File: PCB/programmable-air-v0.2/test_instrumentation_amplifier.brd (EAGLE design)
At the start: 100 x 80 mm, 15 parts, among them IC1 INA126U, IC2 7805T

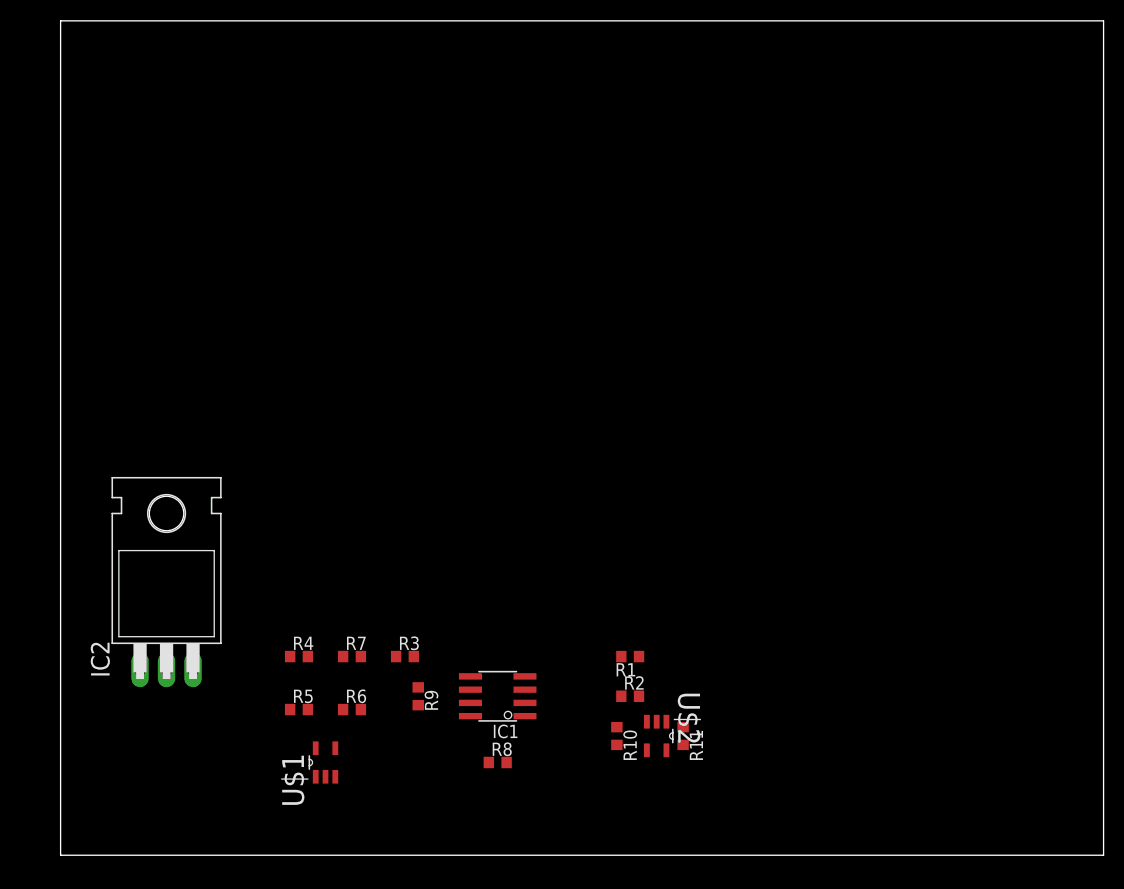
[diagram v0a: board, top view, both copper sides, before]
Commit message: Working towards instrumentation amplifier instead of HX711
MCP6001 was a huge mistake. 6V Vin max. Modifying circuit to LM358.
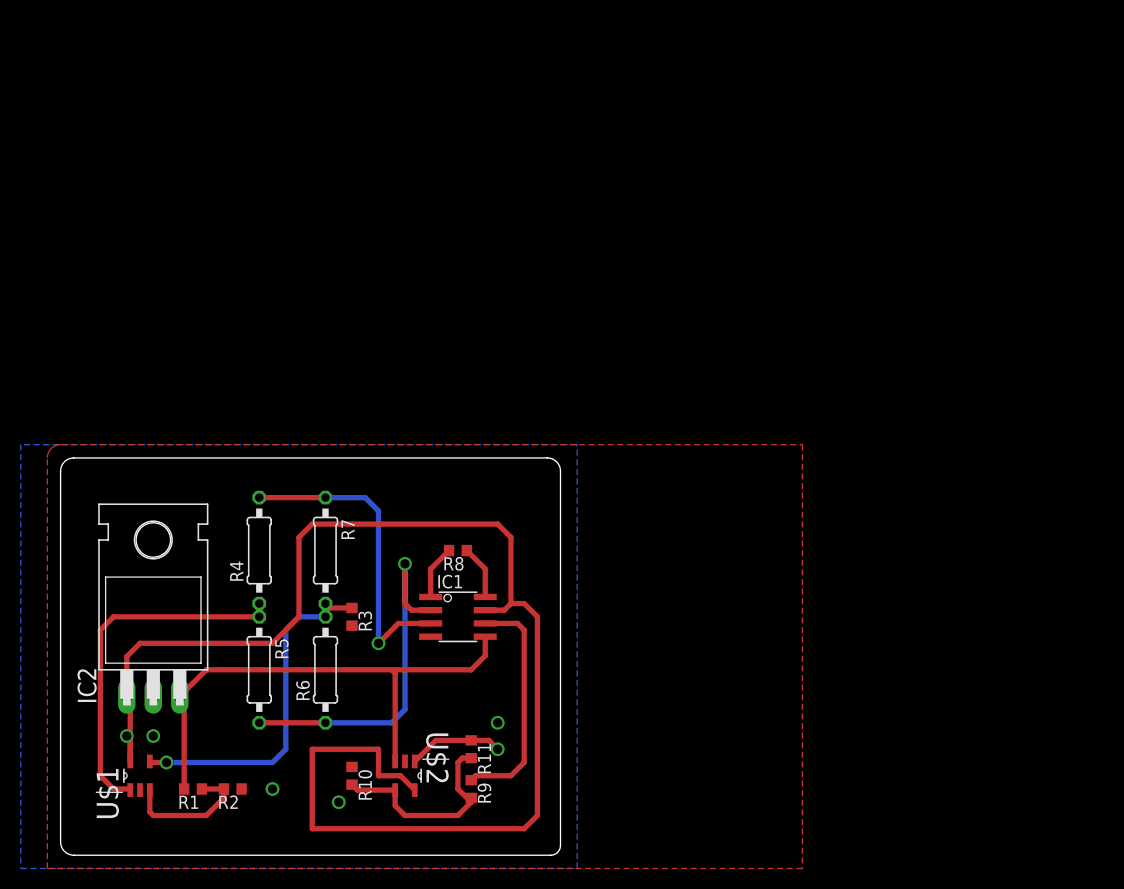
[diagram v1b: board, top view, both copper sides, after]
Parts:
- R4, R5, R6, R7: device eagle-ltspice:R0603 -> eagle-ltspice:0207/10
- moved R1 43.8 mm to (12.7, 6.35)
- moved R2 39.1 mm to (16.5, 6.35), turned to 180 degrees
- moved R10 25.7 mm to (27.9, 7.62)
- moved U$2 24.4 mm to (33.0, 7.62)
- moved R8 20.7 mm to (38.1, 29.2), turned to 180 degrees
- moved R11 20.4 mm to (39.4, 10.2)
- moved U$1 17.8 mm to (7.62, 7.62)
- moved R4 10.9 mm to (19.1, 29.2), turned to 90 degrees
- moved R7 10.5 mm to (25.4, 29.2), turned to 270 degrees
- moved R9 10.2 mm to (39.4, 6.35)
- moved IC1 8.52 mm to (38.1, 22.9), turned to 270 degrees
- moved R3 6.35 mm to (27.9, 22.9), turned to 270 degrees
- moved R5 5.39 mm to (19.1, 17.8), turned to 270 degrees
- moved R6 4.58 mm to (25.4, 17.8), turned to 90 degrees
- moved IC2 2.84 mm to (8.89, 25.4)
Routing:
- net VCC: track 0.00 -> 133.7 mm, vias 0 -> 1
- net N$4: track 0.00 -> 50.7 mm
- net N$7: track 0.00 -> 35.0 mm, vias 0 -> 1
- net N$8: track 0.00 -> 34.4 mm
- net N$6: track 0.00 -> 33.3 mm, vias 0 -> 1
- net N$3: track 0.00 -> 30.4 mm, vias 0 -> 1
- net N$9: track 0.00 -> 22.5 mm
- net N$1: track 0.00 -> 20.3 mm
- net N$10: track 0.00 -> 13.0 mm
- net N$12: track 0.00 -> 9.14 mm, vias 0 -> 1
- net N$5: track 0.00 -> 5.18 mm
- net N$2: track 0.00 -> 5.18 mm
- added copper zone on layer 1, net GND
- added copper zone on layer 16, net GND
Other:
- board size 100 x 80 mm -> 47.9 x 38.1 mm

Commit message: LM358 test board ready
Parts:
- removed R5, R7: 20K, eagle-ltspice:0207/10
- removed R6: 19.9K, eagle-ltspice:0207/10
- removed U$2: MCP6001T-I/OT, MCP6001T-I_OT:SOT95P270X145-5N
- added CN1: 1X4-BIG, adafruit:1X04-BIG
- added IC3: LM358MX, linear:SO08
- added R12, R13: (no value), eagle-ltspice:0207/10
- R1, R10, R11, R2, R3, R8, R9: device eagle-ltspice:R0603 -> eagle-ltspice:0207/10
- R4: value 20K -> 15K
- U$1: value MCP6001T-I/OT -> 2SMPP-03; device MCP6001T-I_OT:SOT95P270X145-5N -> programmable-air-components:2SMPP-03
- moved R4 23.3 mm to (10.2, 7.62)
- moved U$1 22.5 mm to (22.9, 24.1), turned to 180 degrees
- moved R2 14.0 mm to (2.54, 7.62), turned to 270 degrees
- moved R11 13.7 mm to (27.9, 2.54), turned to 180 degrees
- moved R3 11.4 mm to (17.8, 17.8), turned to 0 degrees
- moved R9 7.18 mm to (34.3, 11.4), turned to 180 degrees
- moved R1 6.48 mm to (6.35, 7.62), turned to 90 degrees
- moved R10 6.35 mm to (34.3, 7.62), turned to 180 degrees
- moved R8 5.24 mm to (33.0, 30.5)
- moved IC2 4.58 mm to (6.35, 29.2)
- moved IC1 2.84 mm to (36.8, 25.4)
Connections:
- removed net N$6: R3.1, R6.2, R7.2, U$1.4
- new net N$11: IC3.5, R12.2, R13.1
- new net N$13: IC3.2, R3.2, U$1.P$3
- net GND: now also CN1.4, IC3.4, R12.1, R3.1; no longer R3.2, U$1.2, U$2.2
- net N$1: now also IC3.6; no longer U$2.4
- net N$10: now also IC3.3, R4.1; no longer U$1.3
- net N$12: now also CN1.3, IC3.7; no longer U$2.1
- net N$3: now also U$1.P$4; no longer R4.2, R7.1
- net N$4: now also CN1.2, R13.2, R4.2; no longer U$2.3
- net N$7: now also U$1.P$1; no longer R5.2, R6.1
- net N$8: now also IC3.1, U$1.P$6; no longer R4.1, R5.1, U$1.1
- net VCC: now also CN1.1, IC3.8; no longer U$1.5, U$2.5
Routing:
- net N$12: track 9.14 -> 48.0 mm, vias 1 -> 0
- net N$6: track 33.3 -> 0.00 mm, vias 1 -> 0
- net VCC: track 133.7 -> 108.5 mm, vias 1 -> 0
- net N$13: track 0.00 -> 22.7 mm
- net N$3: track 30.4 -> 8.05 mm
- net N$4: track 50.7 -> 68.3 mm
- net N$8: track 34.4 -> 17.7 mm, vias 0 -> 1
- net N$10: track 13.0 -> 28.6 mm
- net N$11: track 0.00 -> 11.4 mm
- net N$7: track 35.0 -> 23.8 mm
- net N$9: track 22.5 -> 17.2 mm
- net N$1: track 20.3 -> 16.5 mm
- net N$5: track 5.18 -> 8.33 mm
- net N$2: track 5.18 -> 4.15 mm
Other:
- board size 47.9 x 38.1 mm -> 45.4 x 40.6 mm

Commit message: LM358 slave board ready
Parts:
- R1, R4: value 15K -> 30K
- R12, R13: value (none) -> 10K
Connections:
- net N$8: now also U$1.P$5
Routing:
- net N$4: track 68.3 -> 69.6 mm
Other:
- outline, holes or cut-outs redrawn
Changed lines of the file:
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@@
 <board>
 <plain>
-<wire x1="45.39" y1="0" x2="45.39" y2="40.63" width="0" layer="20"/>
-<wire x1="45.39" y1="40.63" x2="0" y2="40.63" width="0" layer="20"/>
-<wire x1="0" y1="40.63" x2="0" y2="0" width="0" layer="20"/>
-<wire x1="0" y1="0" x2="45.39" y2="0" width="0" layer="20"/>
+<wire x1="1.27" y1="0" x2="44.12" y2="0" width="0" layer="20"/>
+<wire x1="44.12" y1="0" x2="45.39" y2="1.27" width="0" layer="20" curve="90"/>
+<wire x1="45.39" y1="1.27" x2="45.39" y2="39.36" width="0" layer="20"/>
+<wire x1="45.39" y1="39.36" x2="44.12" y2="40.63" width="0" layer="20" curve="90"/>
+<wire x1="44.12" y1="40.63" x2="1.27" y2="40.63" width="0" layer="20"/>
+<wire x1="1.27" y1="40.63" x2="0" y2="39.36" width="0" layer="20" curve="90"/>
+<wire x1="0" y1="39.36" x2="0" y2="1.27" width="0" layer="20"/>
+<wire x1="0" y1="1.27" x2="1.27" y2="0" width="0" layer="20" curve="90"/>
 </plain>
 <attributes>
@@
 <attribute name="SPICEPREFIX" value="X" x="6.35" y="29.21" size="1.778" layer="27" display="off"/>
 </element>
-<element name="R1" library="eagle-ltspice" library_urn="urn:adsk.eagle:library:217" package="0207/10" package3d_urn="urn:adsk.eagle:package:13275/1" value="15K" x="6.35" y="7.62" rot="R90">
+<element name="R1" library="eagle-ltspice" library_urn="urn:adsk.eagle:library:217" package="0207/10" package3d_urn="urn:adsk.eagle:package:13275/1" value="30K" x="6.35" y="7.62" rot="R90">
 <attribute name="SPICEMODEL" value="NONE" x="6.35" y="7.62" size="1.778" layer="27" rot="R90" display="off"/>
 <attribute name="SPICEPREFIX" value="R" x="6.35" y="7.62" size="1.778" layer="27" rot="R90" display="off"/>
@@
 </element>
 <element name="IC3" library="linear" library_urn="urn:adsk.eagle:library:262" package="SO08" package3d_urn="urn:adsk.eagle:package:16404/2" value="LM358MX" x="24.13" y="10.16" rot="R180"/>
-<element name="R12" library="eagle-ltspice" library_urn="urn:adsk.eagle:library:217" package="0207/10" package3d_urn="urn:adsk.eagle:package:13275/1" value="" x="17.78" y="7.62" rot="R270">
+<element name="R12" library="eagle-ltspice" library_urn="urn:adsk.eagle:library:217" package="0207/10" package3d_urn="urn:adsk.eagle:package:13275/1" value="10K" x="17.78" y="7.62" rot="R270">
 <attribute name="SPICEMODEL" value="NONE" x="17.78" y="7.62" size="1.778" layer="27" rot="R270" display="off"/>
 <attribute name="SPICEPREFIX" value="R" x="17.78" y="7.62" size="1.778" layer="27" rot="R270" display="off"/>
 </element>
-<element name="R13" library="eagle-ltspice" library_urn="urn:adsk.eagle:library:217" package="0207/10" package3d_urn="urn:adsk.eagle:package:13275/1" value="" x="13.97" y="7.62" rot="R90">
+<element name="R13" library="eagle-ltspice" library_urn="urn:adsk.eagle:library:217" package="0207/10" package3d_urn="urn:adsk.eagle:package:13275/1" value="10K" x="13.97" y="7.62" rot="R90">
 <attribute name="SPICEMODEL" value="NONE" x="13.97" y="7.62" size="1.778" layer="27" rot="R90" display="off"/>
 <attribute name="SPICEPREFIX" value="R" x="13.97" y="7.62" size="1.778" layer="27" rot="R90" display="off"/>
@@
 <element name="U$1" library="programmable-air-components" package="2SMPP-03" value="2SMPP-03" x="22.86" y="24.13" rot="R180"/>
 <element name="CN1" library="adafruit" package="1X04-BIG" value="1X4-BIG" x="33.02" y="35.56"/>
-<element name="R4" library="eagle-ltspice" library_urn="urn:adsk.eagle:library:217" package="0207/10" package3d_urn="urn:adsk.eagle:package:13275/1" value="15K" x="10.16" y="7.62" rot="R90">
+<element name="R4" library="eagle-ltspice" library_urn="urn:adsk.eagle:library:217" package="0207/10" package3d_urn="urn:adsk.eagle:package:13275/1" value="30K" x="10.16" y="7.62" rot="R90">
 <attribute name="SPICEMODEL" value="NONE" x="10.16" y="7.62" size="1.778" layer="27" rot="R90" display="off"/>
 <attribute name="SPICEPREFIX" value="R" x="10.16" y="7.62" size="1.778" layer="27" rot="R90" display="off"/>
@@
 <contactref element="IC2" pad="1"/>
 <contactref element="CN1" pad="1"/>
-<wire x1="33.02" y1="35.56" x2="12.7" y2="35.56" width="0.508" layer="1"/>
-<wire x1="12.7" y1="35.56" x2="3.81" y2="26.67" width="0.508" layer="1"/>
-<wire x1="3.81" y1="26.67" x2="3.81" y2="19.05" width="0.508" layer="1"/>
 <wire x1="33.02" y1="36.83" x2="34.28" y2="38.09" width="0.508" layer="1"/>
 <wire x1="41.92" y1="38.09" x2="43.18" y2="36.83" width="0.508" layer="1"/>
@@
 <wire x1="43.18" y1="5.08" x2="43.18" y2="27.94" width="0.508" layer="1"/>
 <wire x1="26.67" y1="5.08" x2="43.18" y2="5.08" width="0.508" layer="1"/>
+<wire x1="3.81" y1="19.05" x2="3.81" y2="26.67" width="0.508" layer="16"/>
+<wire x1="3.81" y1="26.67" x2="12.7" y2="35.56" width="0.508" layer="16"/>
+<wire x1="12.7" y1="35.56" x2="33.02" y2="35.56" width="0.508" layer="16"/>
 </signal>
 <signal name="N$7">
@@
 <wire x1="29.21" y1="22.86" x2="27.305" y2="22.86" width="0.508" layer="16"/>
 <wire x1="26.67" y1="16.51" x2="30.48" y2="16.51" width="0.508" layer="16"/>
+<contactref element="U$1" pad="P$5"/>
+<wire x1="27.305" y1="22.86" x2="27.305" y2="24.13" width="0" layer="19" extent="16-16"/>
 </signal>
 <signal name="N$3">
@@
 <wire x1="10.16" y1="12.7" x2="6.35" y2="12.7" width="0.508" layer="1"/>
 <wire x1="13.97" y1="12.7" x2="10.16" y2="15.24" width="0.508" layer="1"/>
-<wire x1="8.89" y1="27.94" x2="13.97" y2="33.02" width="0.508" layer="1"/>
-<wire x1="13.97" y1="33.02" x2="34.29" y2="33.02" width="0.508" layer="1"/>
-<wire x1="34.29" y1="33.02" x2="35.56" y2="34.29" width="0.508" layer="1"/>
-<wire x1="35.56" y1="34.29" x2="35.56" y2="35.56" width="0.508" layer="1"/>
-<wire x1="8.89" y1="19.05" x2="8.89" y2="27.94" width="0.508" layer="1"/>
 <wire x1="37.465" y1="23.495" x2="39.4462" y2="23.495" width="0.508" layer="1"/>
 <wire x1="37.465" y1="27.2818375" x2="37.465" y2="23.495" width="0.508" layer="1"/>
 <wire x1="35.56" y1="29.1868375" x2="37.465" y2="27.2818375" width="0.508" layer="1"/>
-<wire x1="35.56" y1="34.29" x2="35.56" y2="29.1868375" width="0.508" layer="1"/>
+<wire x1="35.56" y1="35.56" x2="35.56" y2="29.1868375" width="0.508" layer="1"/>
+<wire x1="8.89" y1="19.05" x2="8.89" y2="27.94" width="0.508" layer="16"/>
+<wire x1="8.89" y1="27.94" x2="13.97" y2="33.02" width="0.508" layer="16"/>
+<wire x1="13.97" y1="33.02" x2="34.29" y2="33.02" width="0.508" layer="16"/>
+<wire x1="34.29" y1="33.02" x2="35.56" y2="34.29" width="0.508" layer="16"/>
+<wire x1="35.56" y1="34.29" x2="35.56" y2="35.56" width="0.508" layer="16"/>
 </signal>
 <signal name="N$10">
@@
 <contactref element="R10" pad="1"/>
 <polygon width="0.1524" layer="1" isolate="0.4064">
-<vertex x="-1.27" y="-1.27"/>
-<vertex x="-1.27" y="38.1" curve="-90"/>
-<vertex x="0" y="39.37"/>
-<vertex x="71.12" y="39.37"/>
-<vertex x="71.12" y="-1.27"/>
-</polygon>
-<polygon width="0.508" layer="16" isolate="0.4064">
-<vertex x="-1.27" y="39.37"/>
-<vertex x="-1.27" y="-1.27"/>
-<vertex x="71.12" y="-1.27"/>
-<vertex x="71.12" y="39.37"/>
+<vertex x="0" y="0"/>
+<vertex x="0" y="39.37" curve="-90"/>
+<vertex x="1.27" y="40.64"/>
+<vertex x="45.72" y="40.64"/>
+<vertex x="45.72" y="0"/>
 </polygon>
 <contactref element="R12" pad="1"/>
@@
 <contactref element="CN1" pad="4"/>
 <polygon width="0.508" layer="16" isolate="0.4064">
-<vertex x="45.72" y="0"/>
+<vertex x="1.27" y="0"/>
+<vertex x="44.45" y="0" curve="90"/>
+<vertex x="45.72" y="1.27"/>
 <vertex x="45.72" y="40.64"/>
 <vertex x="0" y="40.64"/>
-<vertex x="0" y="0"/>
+<vertex x="0" y="1.27" curve="90"/>
 </polygon>
 <contactref element="IC3" pad="4"/>
